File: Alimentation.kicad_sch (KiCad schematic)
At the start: 0 parts

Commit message: Partie écran
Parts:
- added U3: 8205A, Composants_Perso:SOT95P285X140-6N, symbol 8205A:8205A
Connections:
- new net: U3.2, U3.5
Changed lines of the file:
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@@
 	(generator_version "9.0")
 	(paper "A4")
+	(symbol
+		(lib_id "8205A:8205A")
+		(at 91.44 60.96 0)
+		(unit 1)
+		(exclude_from_sim no)
+		(in_bom yes)
+		(on_board yes)
+		(dnp no)
+		(fields_autoplaced yes)
+		(property "Reference" "U3"
+			(at 100.33 58.7628 0)
+			(effects
+				(font
+					(size 1.27 1.27)
+				)
+				(justify left)
+			)
+		)
+		(property "Value" "8205A"
+			(at 100.33 61.3028 0)
+			(effects
+				(font
+					(size 1.27 1.27)
+				)
+				(justify left)
+			)
+		)
+		(property "Footprint" "Composants_Perso:SOT95P285X140-6N"
+			(at 91.44 60.96 0)
+			(effects
+				(font
+					(size 1.27 1.27)
+				)
+				(justify bottom)
+				(hide yes)
+			)
+		)
+		(property "Datasheet" ""
+			(at 91.44 60.96 0)
+			(effects
+				(font
+					(size 1.27 1.27)
+				)
+				(hide yes)
+			)
+		)
+		(property "Description" ""
+			(at 91.44 60.96 0)
+			(effects
+				(font
+					(size 1.27 1.27)
+				)
+				(hide yes)
+			)
+		)
+		(property "MF" "UMW"
+			(at 91.44 60.96 0)
+			(effects
+				(font
+					(size 1.27 1.27)
+				)
+				(justify bottom)
+				(hide yes)
+			)
+		)
+		(property "MAXIMUM_PACKAGE_HEIGHT" "1.40mm"
+			(at 91.44 60.96 0)
+			(effects
+				(font
+					(size 1.27 1.27)
+				)
+				(justify bottom)
+				(hide yes)
+			)
+		)
+		(property "Package" "SOT-23-6 UMW"
+			(at 91.44 60.96 0)
+			(effects
+				(font
+					(size 1.27 1.27)
+				)
+				(justify bottom)
+				(hide yes)
+			)
+		)
+		(property "Price" "None"
+			(at 91.44 60.96 0)
+			(effects
+				(font
+					(size 1.27 1.27)
+				)
+				(justify bottom)
+				(hide yes)
+			)
+		)
+		(property "Check_prices" "https://www.snapeda.com/parts/8205A/UMW/view-part/?ref=eda"
+			(at 91.44 60.96 0)
+			(effects
+				(font
+					(size 1.27 1.27)
+				)
+				(justify bottom)
+				(hide yes)
+			)
+		)
+		(property "STANDARD" "IPC 7351B"
+			(at 91.44 60.96 0)
+			(effects
+				(font
+					(size 1.27 1.27)
+				)
+				(justify bottom)
+				(hide yes)
+			)
+		)
+		(property "PARTREV" "NA"
+			(at 91.44 60.96 0)
+			(effects
+				(font
+					(size 1.27 1.27)
+				)
+				(justify bottom)
+				(hide yes)
+			)
+		)
+		(property "SnapEDA_Link" "https://www.snapeda.com/parts/8205A/UMW/view-part/?ref=snap"
+			(at 91.44 60.96 0)
+			(effects
+				(font
+					(size 1.27 1.27)
+				)
+				(justify bottom)
+				(hide yes)
+			)
+		)
+		(property "MP" "8205A"
+			(at 91.44 60.96 0)
+			(effects
+				(font
+					(size 1.27 1.27)
+				)
+				(justify bottom)
+				(hide yes)
+			)
+		)
+		(property "Description_1" "Mosfet Array 20V 5A 830mW (Ta) Surface Mount SOT-23-6"
+			(at 91.44 60.96 0)
+			(effects
+				(font
+					(size 1.27 1.27)
+				)
+				(justify bottom)
+				(hide yes)
+			)
+		)
+		(property "Availability" "In Stock"
+			(at 91.44 60.96 0)
+			(effects
+				(font
+					(size 1.27 1.27)
+				)
+				(justify bottom)
+				(hide yes)
+			)
+		)
+		(property "MANUFACTURER" "UMW"
+			(at 91.44 60.96 0)
+			(effects
+				(font
+					(size 1.27 1.27)
+				)
+				(justify bottom)
+				(hide yes)
+			)
+		)
+		(pin "6"
+		)
+		(pin "3"
+		)
+		(pin "1"
+		)
+		(pin "4"
+		)
+		(pin "2"
+		)
+		(pin "5"
+		)
+		(instances
+			(project "Station_Meteo_pcb"
+				(path "/90bd0b60-6e70-43e1-8410-99fb54688c17/46b21e09-ea67-4534-a48d-e2dad69aede0"
+					(reference "U3")
+					(unit 1)
+				)
+			)
+		)
+	)
 )

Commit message: Début de la partie alimentation
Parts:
- added C13, C15: 22u, symbol Device:C_Small
- added L2: 470n, symbol Device:L
- added Q3: NMOS, symbol Simulation_SPICE:NMOS
- added Q4: PMOS, symbol Simulation_SPICE:PMOS
- added R10: 100k, symbol Device:R
- added R11: 511k, symbol Device:R
- added R12: 91k, symbol Device:R
- added R8, R9: R, symbol Device:R
- added U4: TPS63802DLAR, TPS63802DLAR:VREG_TPS63802DLAR, symbol TPS63802DLAR:TPS63802DLAR
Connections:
- new net: Q3.1 (D), Q4.2 (G), R8.2
- new net: L2.1, U4.9 (L1)
- new net: L2.2, U4.7 (L2)
- new net: R11.2, R12.1, U4.4 (FB)
- new net: R10.2, U4.5 (PG)
- new net +3.3V: Q4.3 (S), R8.1
- new net CMD_ALIM_SCREEN: Q3.2 (G), R9.1
- new net EPD_PWR: Q4.1 (D)
- new net GND: C13.2, C15.2, Q3.3 (S), R12.2, R9.2, U4.2 (MODE), U4.3 (AGND), U4.8 (GND)
- new net VIN: C13.1, U4.1 (EN), U4.10 (VIN)
- new net VOUT: C15.1, R10.1, R11.1, U4.6 (VOUT)
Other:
- note added: "Alimenation écran"
- note added: "Buckboost"
- moved on the sheet: U3

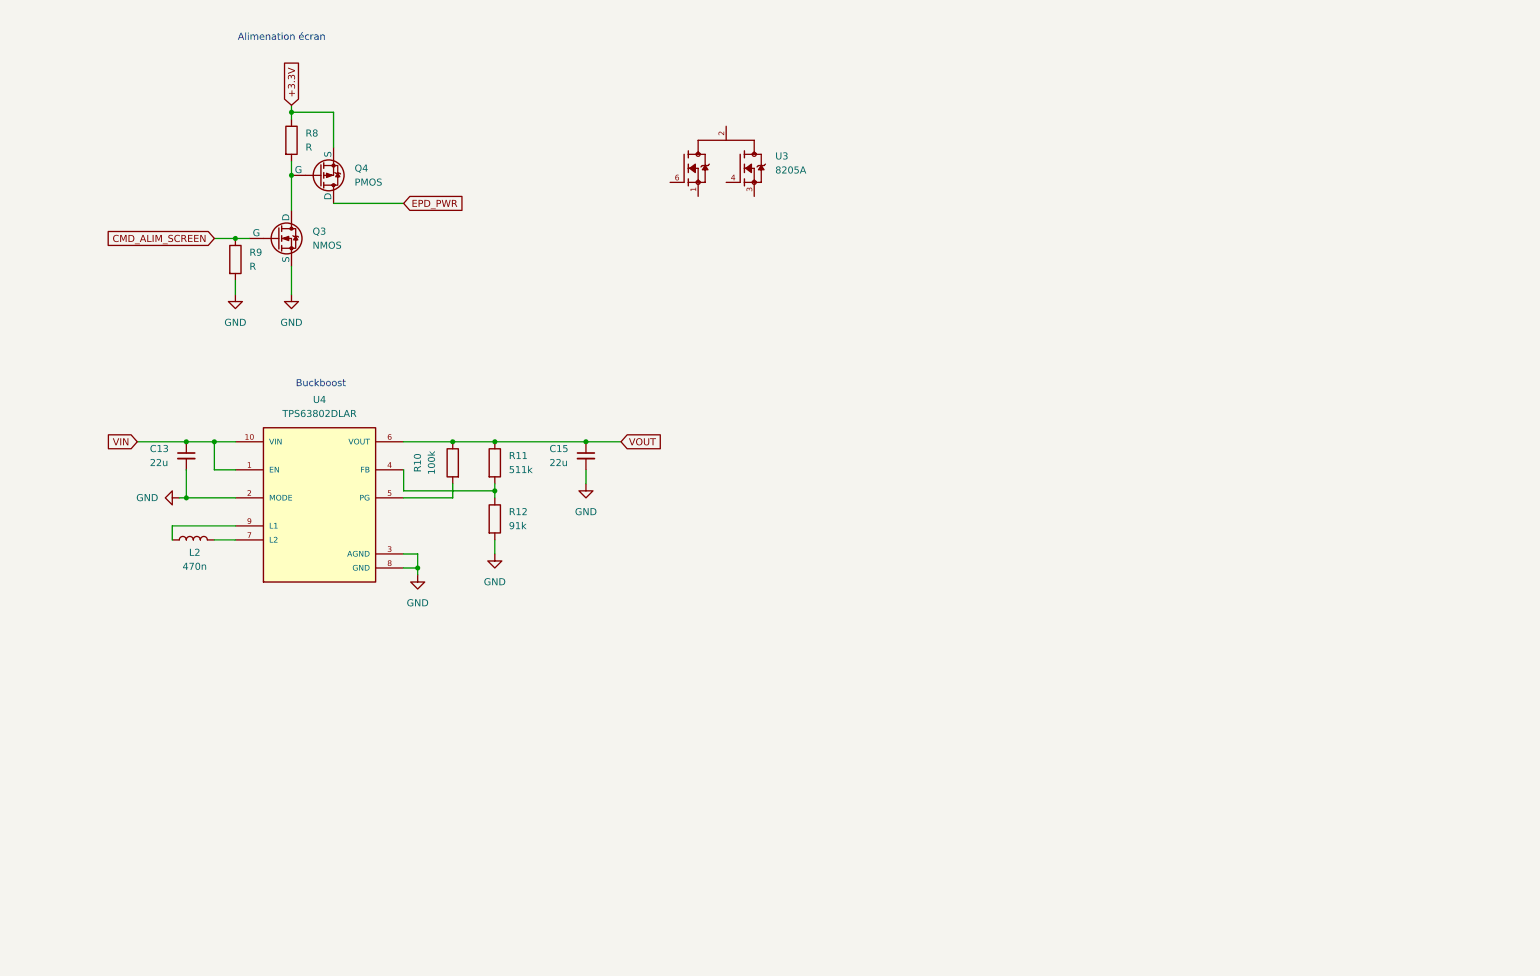
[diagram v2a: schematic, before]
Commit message: Ajout total de la partie alimentation
Ajout de composant depuis un site internet ->OK
Fin de la partie écran et alimentation : ajout de tous les composants
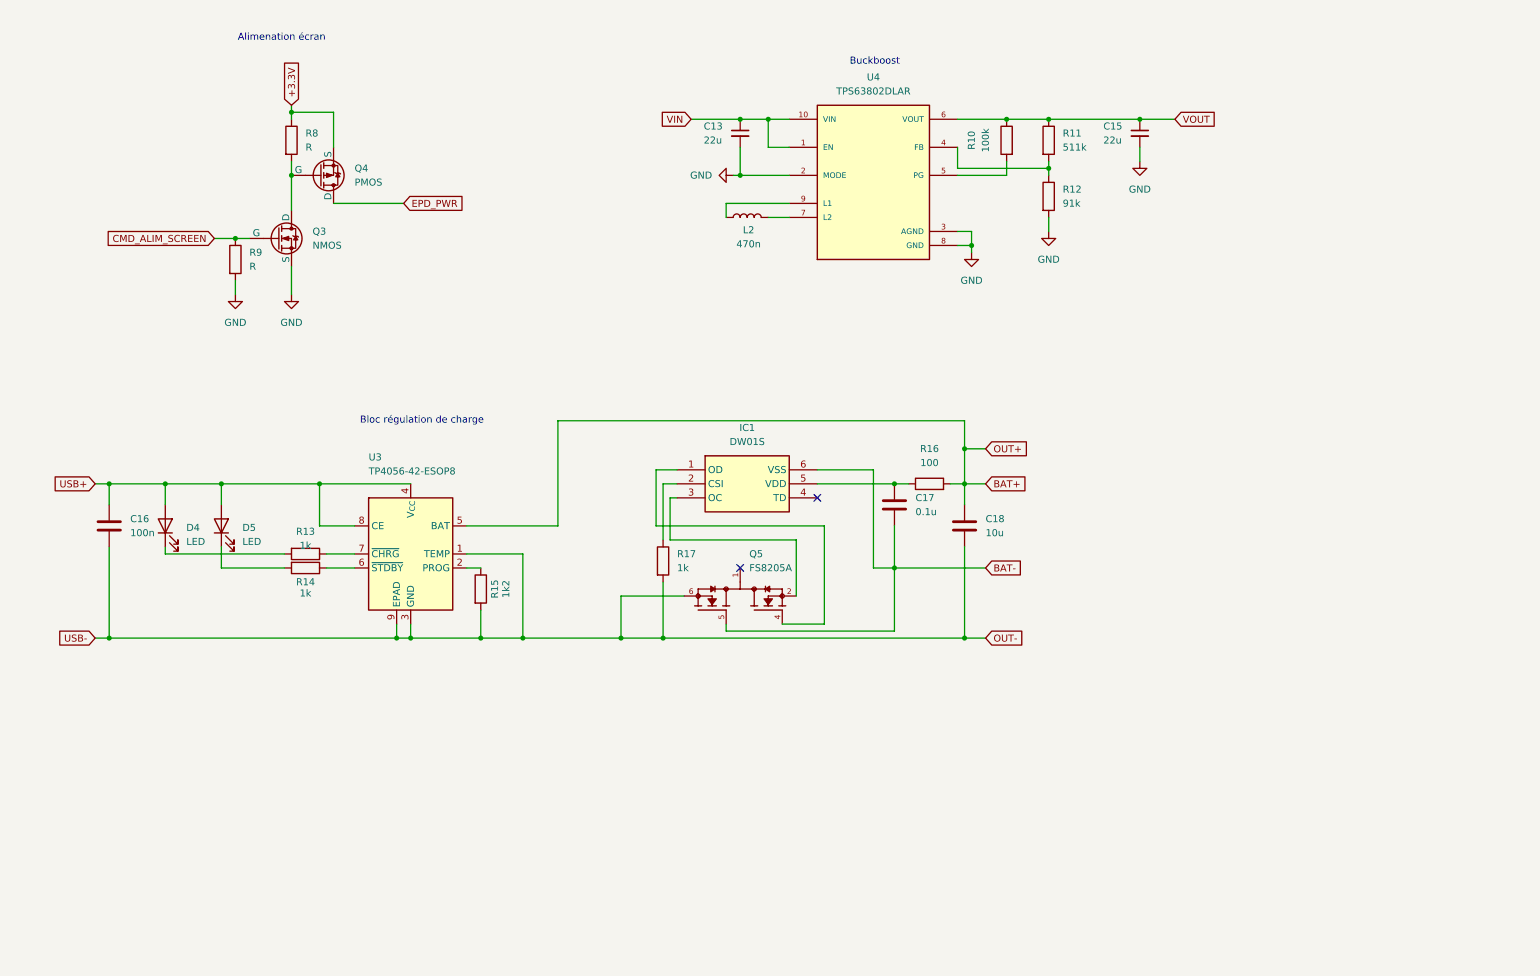
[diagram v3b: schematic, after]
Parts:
- removed U3: 8205A, Composants_Perso:SOT95P285X140-6N, symbol 8205A:8205A
- added C16: 100n, symbol Device:C
- added C17: 0.1u, symbol Device:C
- added C18: 10u, symbol Device:C
- added D4, D5: LED, symbol Device:LED
- added IC1: DW01S, Composants_Perso:DW01S, symbol DW01S:DW01S
- added Q5: FS8205A, Composants_Perso:FS8205A, symbol FS8205A:FS8205A
- added R13, R14, R17: 1k, symbol Device:R
- added R15: 1k2, symbol Device:R
- added R16: 100, symbol Device:R
- added U3: TP4056-42-ESOP8, Package_SO:SOIC-8-1EP_3.9x4.9mm_P1.27mm_EP2.41x3.3mm_ThermalVias, symbol Battery_Management:TP4056-42-ESOP8
- U4: footprint TPS63802DLAR:VREG_TPS63802DLAR -> Composants_Perso:VREG_TPS63802DLAR
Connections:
- new net: D4.1 (K), R13.2
- new net: R14.1, U3.6 (~{STDBY})
- new net: D5.1 (K), R14.2
- new net: C17.1, IC1.5 (VDD), R16.1
- new net: IC1.2 (CSI), R17.1
- new net: Q5.1, Q5.8
- new net: IC1.3 (OC), Q5.2, Q5.3
- new net: IC1.1 (OD), Q5.4
- new net: R13.1, U3.7 (~{CHRG})
- new net: R15.1, U3.2 (PROG)
- new net BAT+: C18.1, R16.2, U3.5 (BAT)
- new net BAT-: C17.2, IC1.6 (VSS), Q5.5
- new net OUT-: C16.2, C18.2, Q5.6, Q5.7, R15.2, R17.2, U3.1 (TEMP), U3.3 (GND), U3.9 (EPAD)
- new net USB+: C16.1, D4.2 (A), D5.2 (A), U3.4 (V_{CC}), U3.8 (CE)
- no-connect marks 0 -> 2
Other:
- note added: "Bloc régulation de charge"
- moved on the sheet: C13, C15, L2, R10, R11, R12

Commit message: Dernieres pour review
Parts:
- added Q6: NMOS, symbol Simulation_SPICE:NMOS
- added Q8: PMOS, symbol Simulation_SPICE:PMOS
- added R21, R22, R23, R24: R, symbol Device:R
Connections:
- net +3.3V: now also Q8.3 (S), R22.1
- net GND: now also Q6.3 (S), R21.2, R24.2
- new net: Q8.1 (D), R23.1
- new net: Q6.1 (D), Q8.2 (G), R22.2
- new net CMD_ALIM_BATTERY: Q6.2 (G), R21.1
- new net MEASURE_BATTERY: R23.2, R24.1
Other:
- note added: "Alimenation batterie"
- moved on the sheet: C13, C15, L2, Q3, Q4, R10, R11, R12, R8, R9, U4

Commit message: revue schema
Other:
- note added: "1Mohm"
- note added: "1Mohm si pb 100k"
- note added: "1Mohm si pb 47k"
- note added: "On va regrouper les labels usb- et out- sur GND pour qu'ils soient regroupé sur le schéma"
- note added: "calculer PDDT pour que 4.2V -> >3.3V"
- note added: "j'ai l'impression que les signaux 2 et 5 du 8205 sont inversés"
- note added: "pas 3.3V mais out+"
- note added: "prévoir R16 au moins 1/4W"
- note added: "rajouter mosfet + diode pour la recharge en utilisation"
- note added: "rajouter une 10uF pour etre safe"
- note added: "regrouper sur un seul label"
- note added: "vérif valeur R en fonction de la ref de LED choisi"
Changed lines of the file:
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@@
 	(generator_version "9.0")
 	(paper "A4")
+	(text "pas 3.3V mais out+"
+		(exclude_from_sim no)
+		(at 241.808 23.114 0)
+		(effects
+			(font
+				(size 1.27 1.27)
+				(color 255 0 0 1)
+			)
+		)
+	)
+	(text "1Mohm"
+		(exclude_from_sim no)
+		(at 217.932 34.798 0)
+		(effects
+			(font
+				(size 1.27 1.27)
+			)
+		)
+	)
+	(text "1Mohm\nsi pb 47k"
+		(exclude_from_sim no)
+		(at 41.148 39.624 0)
+		(effects
+			(font
+				(size 1.27 1.27)
+			)
+		)
+	)
+	(text "On va regrouper les labels usb- et out- sur GND pour qu'ils soient regroupé sur le schéma"
+		(exclude_from_sim no)
+		(at 105.156 138.43 0)
+		(effects
+			(font
+				(size 1.27 1.27)
+				(color 255 0 0 1)
+			)
+		)
+	)
 	(text "Alimenation écran\n"
 		(exclude_from_sim no)
 		(at 46.482 20.828 0)
+		(effects
+			(font
+				(size 1.27 1.27)
+			)
+		)
+	)
+	(text "regrouper sur un seul label"
+		(exclude_from_sim no)
+		(at 197.612 98.552 0)
+		(effects
+			(font
+				(size 1.27 1.27)
+				(color 255 0 0 1)
+			)
+		)
+	)
+	(text "prévoir R16\nau moins 1/4W"
+		(exclude_from_sim no)
+		(at 166.37 93.726 0)
 		(effects
 			(font
@@
 		)
 	)
+	(text "j'ai l'impression que les signaux\n2 et 5 du 8205 sont inversés"
+		(exclude_from_sim no)
+		(at 145.796 132.334 0)
+		(effects
+			(font
+				(size 1.27 1.27)
+				(color 255 0 0 1)
+			)
+		)
+	)
 	(text "Buckboost\n"
 		(exclude_from_sim no)
@@
 			(font
 				(size 1.27 1.27)
+			)
+		)
+	)
+	(text "1Mohm\nsi pb 100k"
+		(exclude_from_sim no)
+		(at 29.972 62.738 0)
+		(effects
+			(font
+				(size 1.27 1.27)
+			)
+		)
+	)
+	(text "calculer PDDT\npour que 4.2V ->  >3.3V"
+		(exclude_from_sim no)
+		(at 270.256 57.658 0)
+		(effects
+			(font
+				(size 1.27 1.27)
+				(color 255 0 0 1)
+			)
+		)
+	)
+	(text "rajouter une 10uF pour etre safe"
+		(exclude_from_sim no)
+		(at 29.464 117.856 0)
+		(effects
+			(font
+				(size 1.27 1.27)
+				(color 255 0 0 1)
 			)
 		)
@@
 			)
 		)
+	)
+	(text "rajouter mosfet + diode pour la recharge en utilisation"
+		(exclude_from_sim no)
+		(at 119.888 83.566 0)
+		(effects
+			(font
+				(size 1.27 1.27)
+				(color 255 0 0 1)
+			)
+		)
+	)
+	(text "1Mohm"
+		(exclude_from_sim no)
+		(at 208.28 57.15 0)
+		(effects
+			(font
+				(size 1.27 1.27)
+			)
+		)
+	)
+	(text "vérif valeur R en fonction de la ref de LED choisi"
+		(exclude_from_sim no)
+		(at 48.26 124.206 0)
+		(effects
+			(font
+				(size 1.27 1.27)
+				(color 255 0 0 1)
+			)
+		)

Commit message: t
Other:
- note added: "rajouter connecteur USB C"
- note added: "rajouter connecteur bloc pile"
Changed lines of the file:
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@@
 			(font
 				(size 1.27 1.27)
+				(color 255 0 0 1)
 			)
 		)
@@
 			)
 		)
+	)
+	(text "rajouter connecteur bloc pile"
+		(exclude_from_sim no)
+		(at 215.138 108.712 0)
+		(effects
+			(font
+				(size 1.27 1.27)
+				(color 255 0 0 1)
+			)
+		)
+	)
+	(text "rajouter connecteur USB C"
+		(exclude_from_sim no)
+		(at 27.686 94.996 0)
+		(effects
+			(font
+				(size 1.27 1.27)
+				(color 255 0 0 1)
+			)
+		)

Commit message: premieres modif depuis la review
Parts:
- added C29: 10u, symbol Device:C
- added D6: 1N5817, Diode_THT:D_DO-41_SOD81_P10.16mm_Horizontal, symbol Diode:1N5817
- added Q2: PMOS, symbol Simulation_SPICE:PMOS
- added R6: 100k, symbol Device:R
- R21, R22, R8, R9: value R -> 1M
- R23: value R -> 100k
- R24: value R -> 330K
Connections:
- net +3.3V: no longer Q8.3 (S), R22.1
- net BAT+: now also Q8.3 (S), R22.1, Q2.1 (D)
- net GND: now also R6.1
- net OUT-: now also C29.1
- net USB+: now also C29.2, D6.2 (A), Q2.2 (G), R6.2
- net VIN: now also D6.1 (K), Q2.3 (S)
- net VOUT renamed +3V3
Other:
- note added: "A vérifier si c'est bien come ça"
- note removed: "1Mohm"
- note removed: "1Mohm si pb 100k"
- note removed: "1Mohm si pb 47k"
- note removed: "calculer PDDT pour que 4.2V -> >3.3V"
- note removed: "pas 3.3V mais out+"
- note removed: "rajouter mosfet + diode pour la recharge en utilisation"
- note removed: "rajouter une 10uF pour etre safe"
- moved on the sheet: R23, R24

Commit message: t
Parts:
- C17: value 0.1u -> 100n
- R23: value 100k -> 10k
- R24: value 330K -> 33K
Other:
- note removed: "A vérifier si c'est bien come ça"
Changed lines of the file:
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@@
 		)
 	)
-	(text "A vérifier si c'est bien come ça"
-		(exclude_from_sim no)
-		(at 180.086 28.448 0)
-		(effects
-			(font
-				(size 1.27 1.27)
-				(color 255 0 2 1)
-			)
-		)
-	)
 	(text "vérif valeur R en fonction de la ref de LED choisi"
 		(exclude_from_sim no)
@@
 			)
 		)
-		(property "Value" "330K"
+		(property "Value" "33K"
 			(at 255.27 54.6099 0)
 			(effects
@@
 			)
 		)
-		(property "Value" "100k"
+		(property "Value" "10k"
 			(at 245.11 41.91 90)
 			(effects
@@
 			)
 		)
-		(property "Value" "0.1u"
+		(property "Value" "100n"
 			(at 173.99 106.6799 0)
 			(effects
